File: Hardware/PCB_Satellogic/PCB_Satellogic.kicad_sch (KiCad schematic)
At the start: 4 parts, among them U1 E22-900M30S_LoRa, U2 Node-MCU_ESP32_38PINES, U3 TP4065_Modulo_cargador_de_bat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

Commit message: Introducción HW
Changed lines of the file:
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@@
-(kicad_sch (version 20211123) (generator eeschema)
+(kicad_sch (version 20230121) (generator eeschema)
   (paper "A4")
   (symbol (lib_id "Device:E22-900M30S_LoRa") (at 124.46 68.58 0) (unit 1)
-    (in_bom yes) (on_board yes)
-    (property "Reference" "U1" (id 0) (at 124.46 47.879 0))
-    (property "Value" "E22-900M30S_LoRa" (id 1) (at 124.46 50.1904 0))
-    (property "Footprint" "PCB_Satellogic:E22-900M30S_LoRa_smd" (id 2) (at 123.19 60.96 0)
+    (in_bom yes) (on_board yes) (dnp no)
+    (property "Reference" "U1" (at 124.46 47.879 0)
+      (effects (font (size 1.27 1.27)))
+    )
+    (property "Value" "E22-900M30S_LoRa" (at 124.46 50.1904 0)
+      (effects (font (size 1.27 1.27)))
+    )
+    (property "Footprint" "PCB_Satellogic:E22-900M30S_LoRa_smd" (at 123.19 60.96 0)
       (effects (font (size 1.27 1.27)) hide)
     )
-    (property "Datasheet" "" (id 3) (at 123.19 60.96 0)
+    (property "Datasheet" "" (at 123.19 60.96 0)
       (effects (font (size 1.27 1.27)) hide)
     )
@@
     (pin "8")
     (pin "9")
+    (instances
+      (project "PCB_Satellogic"
+        (path "/1c395ffa-f49b-425d-a435-d93dd675dfd0"
+          (reference "U1") (unit 1)
+        )
+      )
+    )
+  )
+  (symbol (lib_id "Diode:1N5819") (at 149.86 81.28 180) (unit 1)
+    (in_bom yes) (on_board yes) (dnp no) (fields_autoplaced)
+    (property "Reference" "D1" (at 150.1775 76.2 0)
+      (effects (font (size 1.27 1.27)))
+    )
+    (property "Value" "1N5819" (at 150.1775 78.74 0)
+      (effects (font (size 1.27 1.27)))
+    )
+    (property "Footprint" "Diode_THT:D_DO-41_SOD81_P10.16mm_Horizontal" (at 149.86 76.835 0)
+      (effects (font (size 1.27 1.27)) hide)
+    )
+    (property "Datasheet" "http://www.vishay.com/docs/88525/1n5817.pdf" (at 149.86 81.28 0)
+      (effects (font (size 1.27 1.27)) hide)
+    )
+    (pin "1")
+    (pin "2")
+    (instances
+      (project "PCB_Satellogic"
+        (path "/1c395ffa-f49b-425d-a435-d93dd675dfd0"
+          (reference "D1") (unit 1)
+        )
+      )
+    )
   )
   (symbol (lib_id "Device:Node-MCU_ESP32_38PINES") (at 172.72 57.15 0) (unit 1)
-    (in_bom yes) (on_board yes)
-    (property "Reference" "U2" (id 0) (at 172.72 28.829 0))
-    (property "Value" "Node-MCU_ESP32_38PINES" (id 1) (at 172.72 31.1404 0))
-    (property "Footprint" "PCB_Satellogic:Node-MCU_ESP32_38PINES_THT_offset" (id 2) (at 180.34 68.58 0)
+    (in_bom yes) (on_board yes) (dnp no) (fields_autoplaced)
+    (property "Reference" "U2" (at 172.72 29.21 0)
+      (effects (font (size 1.27 1.27)))
+    )
+    (property "Value" "Node-MCU_ESP32_38PINES" (at 172.72 31.75 0)
+      (effects (font (size 1.27 1.27)))
+    )
+    (property "Footprint" "PCB_Satellogic:Node-MCU_ESP32_38PINES_THT_offset" (at 180.34 68.58 0)
       (effects (font (size 1.27 1.27)) hide)
     )
-    (property "Datasheet" "" (id 3) (at 180.34 68.58 0)
+    (property "Datasheet" "" (at 180.34 68.58 0)
       (effects (font (size 1.27 1.27)) hide)
     )
@@
     (pin "8")
     (pin "9")
+    (instances
+      (project "PCB_Satellogic"
+        (path "/1c395ffa-f49b-425d-a435-d93dd675dfd0"
+          (reference "U2") (unit 1)
+        )
+      )
+    )
   )
-  (symbol (lib_id "Diode:1N5819") (at 147.32 81.28 180) (unit 1)
-    (in_bom yes) (on_board yes) (fields_autoplaced)
-    (property "Reference" "D1" (id 0) (at 147.6375 74.93 0))
-    (property "Value" "1N5819" (id 1) (at 147.6375 77.47 0))
-    (property "Footprint" "Diode_THT:D_DO-41_SOD81_P10.16mm_Horizontal" (id 2) (at 147.32 76.835 0)
+  (symbol (lib_id "Libreria_Proyecto_Satellogic:TP4065_Modulo_cargador_de_baterias") (at 72.39 73.66 0) (unit 1)
+    (in_bom yes) (on_board yes) (dnp no) (fields_autoplaced)
+    (property "Reference" "U3" (at 72.39 60.96 0)
+      (effects (font (size 1.27 1.27)))
+    )
+    (property "Value" "TP4065_Modulo_cargador_de_baterias" (at 72.39 63.5 0)
+      (effects (font (size 1.27 1.27)))
+    )
+    (property "Footprint" "PCB_Satellogic:TP4056" (at 71.12 68.58 0)
       (effects (font (size 1.27 1.27)) hide)
     )
-    (property "Datasheet" "http://www.vishay.com/docs/88525/1n5817.pdf" (id 3) (at 147.32 81.28 0)
-      (effects (font (size 1.27 1.27)) hide)
-    )
-    (pin "1")
-    (pin "2")
-  )
-  (symbol (lib_id "Libreria_Proyecto_Satellogic:TP4065_Modulo_cargador_de_baterias") (at 62.23 72.39 0) (unit 1)
-    (in_bom yes) (on_board yes) (fields_autoplaced)
-    (property "Reference" "U3" (id 0) (at 62.23 58.42 0))
-    (property "Value" "TP4065_Modulo_cargador_de_baterias" (id 1) (at 62.23 60.96 0))
-    (property "Footprint" "PCB_Satellogic:TP4056" (id 2) (at 60.96 67.31 0)
-      (effects (font (size 1.27 1.27)) hide)
-    )
-    (property "Datasheet" "" (id 3) (at 60.96 67.31 0)
+    (property "Datasheet" "" (at 71.12 68.58 0)
       (effects (font (size 1.27 1.27)) hide)
     )
@@
     (pin "5")
     (pin "6")
+    (instances
+      (project "PCB_Satellogic"
+        (path "/1c395ffa-f49b-425d-a435-d93dd675dfd0"
+          (reference "U3") (unit 1)
+        )
+      )
+    )
   )
   (sheet_instances
     (path "/" (page "1"))
   )
-  (symbol_instances
-    (path "/9dc25e6c-ccc6-4fa7-a0b9-7dc1baf8ff68"
-      (reference "D1") (unit 1) (value "1N5819") (footprint "Diode_THT:D_DO-41_SOD81_P10.16mm_Horizontal")
-    )
-    (path "/00000000-0000-0000-0000-0000640a4933"
-      (reference "U1") (unit 1) (value "E22-900M30S_LoRa") (footprint "PCB_Satellogic:E22-900M30S_LoRa_smd")
-    )
-    (path "/00000000-0000-0000-0000-0000640a5209"
-      (reference "U2") (unit 1) (value "Node-MCU_ESP32_38PINES") (footprint "PCB_Satellogic:Node-MCU_ESP32_38PINES_THT_offset")
-    )
-    (path "/db130f58-7442-4364-94e7-fd26116f26ed"
-      (reference "U3") (unit 1) (value "TP4065_Modulo_cargador_de_baterias") (footprint "PCB_Satellogic:TP4056")
-    )
-  )
 )

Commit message: Introducción HW
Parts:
- removed U2: Node-MCU_ESP32_38PINES, PCB_Satellogic:Node-MCU_ESP32_38PINES_THT_offset, symbol Device:Node-MCU_ESP32_38PINES
- added 5V_out1, BAT1, UART2: Conn_01x02, Connector_JST:JST_PH_B2B-PH-K_1x02_P2.00mm_Vertical, symbol Connector_Generic:Conn_01x02
- added U2: Node-MCU_ESP32_38PINES, PCB_Satellogic:Node-MCU_ESP32_38PINES_THT_offset, symbol Libreria_Proyecto_Satellogic:Node-MCU_ESP32_38PINES
- added U4: MT3608-Convertidor_Boost, PCB_Satellogic:MT3608-Convertidor_Boost, symbol Libreria_Proyecto_Satellogic:MT3608-Convertidor_Boost
- U3: footprint PCB_Satellogic:TP4056 -> PCB_Satellogic:TP4056 - Módulo de carga de batería
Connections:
- net GND: now reaches U1.1 (GND)
- net GND: now also U1.11 (GND), U1.12 (GND), U1.2 (GND), U1.20 (GND), U1.22 (GND), U1.3 (GND), U1.4 (GND), U1.5 (GND), 5V_out1.2 (Pin_2), U2.14 (GND), U2.38 (GND), U4.2 (VOUT-)
- net 5V: now reaches U1.10 (Vcc)
- net 5V: now also D1.2 (A), U1.9 (Vcc), 5V_out1.1 (Pin_1), U4.1 (VOUT+)
- net BUSY: now reaches U1.14 (BUSY)
- net BUSY: now also U2.33 (GPIO21)
- net RST_E22: now reaches U1.15 (NRST)
- net RST_E22: now also U2.36 (GPIO22)
- net MISO: now reaches U1.16 (MISO)
- net MISO: now also U2.31 (MISO-GPIO19)
- net MOSI: now reaches U1.17 (MOSI)
- net MOSI: now also U2.37 (MOSI-GPIO23)
- net SCK: now reaches U1.18 (SCK)
- net SCK: now also U2.30 (CLK-GPIO18)
- net NSS: now reaches U1.19 (NSS)
- net NSS: now also U2.29 (CS0-GPIO5)
- net RXEN: now reaches U1.6 (RXEN)
- net TXEN: now reaches U1.7 (TXEN)
- net at D1.1 (K): now also U2.19 (Vin)
- net at U3.3 (OUT-): now also U4.3 (VIN-)
- net BAT-: now reaches U3.4 (BAT-)
- net BAT-: now also BAT1.2 (Pin_2)
- net BAT+: now reaches U3.5 (BAT+)
- net BAT+: now also BAT1.1 (Pin_1)
- net at U3.6 (OUT+): now also U4.4 (VIN+)
- new net Rx2: U2.27 (Rx2-GPIO16), UART2.2 (Pin_2)
- new net Tx2: U2.28 (Tx2-GPIO17), UART2.1 (Pin_1)
- no-connect marks 0 -> 32
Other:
- company: (none) -> Satellogic
- title: (none) -> Esquema dispositivo de comunicación ESP32-E22
- moved on the sheet: D1, U1, U3

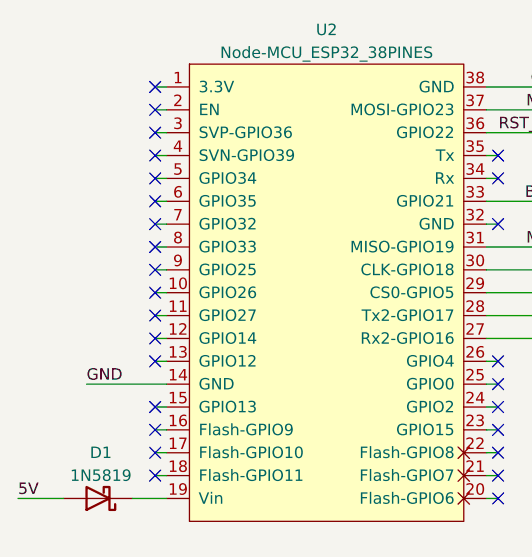
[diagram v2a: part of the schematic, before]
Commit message: Se agregó función para ver registros
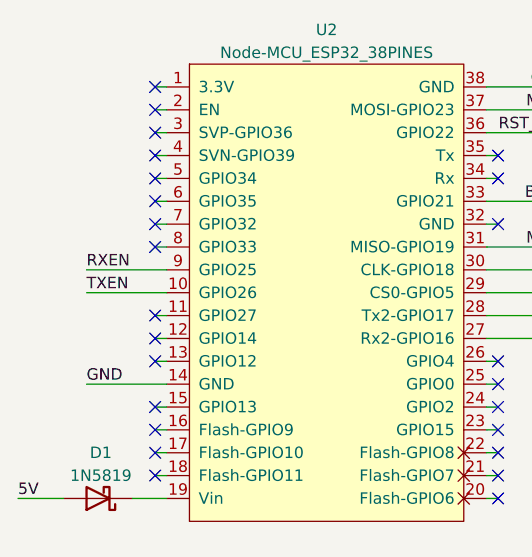
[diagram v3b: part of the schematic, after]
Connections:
- net RXEN: now also U2.9 (GPIO25)
- net TXEN: now also U2.10 (GPIO26)
- no-connect marks 32 -> 30
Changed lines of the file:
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@@
     (company "Satellogic")
   )
-  (no_connect (at 60.96 60.96))
   (no_connect (at 60.96 43.18))
   (no_connect (at 60.96 63.5))
@@
   (no_connect (at 60.96 55.88))
   (no_connect (at 99.06 76.2))
-  (no_connect (at 60.96 58.42))
   (no_connect (at 60.96 40.64))
   (no_connect (at 99.06 45.72))
@@
     (stroke (width 0) (type default))
   )
+  (wire (pts (xy 53.34 58.42) (xy 62.23 58.42))
+    (stroke (width 0) (type default))
+  )
   (wire (pts (xy 219.71 38.1) (xy 232.41 38.1))
     (stroke (width 0) (type default))
@@
     (stroke (width 0) (type default))
   )
+  (wire (pts (xy 53.34 60.96) (xy 62.23 60.96))
+    (stroke (width 0) (type default))
+  )
   (wire (pts (xy 99.06 73.66) (xy 97.79 73.66))
     (stroke (width 0) (type default))
@@
     (stroke (width 0) (type default))
   )
-  (wire (pts (xy 60.96 58.42) (xy 62.23 58.42))
-    (stroke (width 0) (type default))
-  )
   (wire (pts (xy 60.96 76.2) (xy 62.23 76.2))
     (stroke (width 0) (type default))
@@
     (stroke (width 0) (type default))
   )
-  (wire (pts (xy 60.96 60.96) (xy 62.23 60.96))
-    (stroke (width 0) (type default))
-  )
   (wire (pts (xy 97.79 63.5) (xy 106.68 63.5))
     (stroke (width 0) (type default))
@@
     (effects (font (size 1.27 1.27)) (justify left bottom))
   )
+  (label "TXEN" (at 53.34 60.96 0) (fields_autoplaced)
+    (effects (font (size 1.27 1.27)) (justify left bottom))
+  )
   (label "GND" (at 100.33 121.92 180) (fields_autoplaced)
     (effects (font (size 1.27 1.27)) (justify right bottom))
@@
     (effects (font (size 1.27 1.27)) (justify right bottom))
   )
+  (label "RXEN" (at 53.34 58.42 0) (fields_autoplaced)
+    (effects (font (size 1.27 1.27)) (justify left bottom))
+  )
   (label "GND" (at 100.33 127 180) (fields_autoplaced)

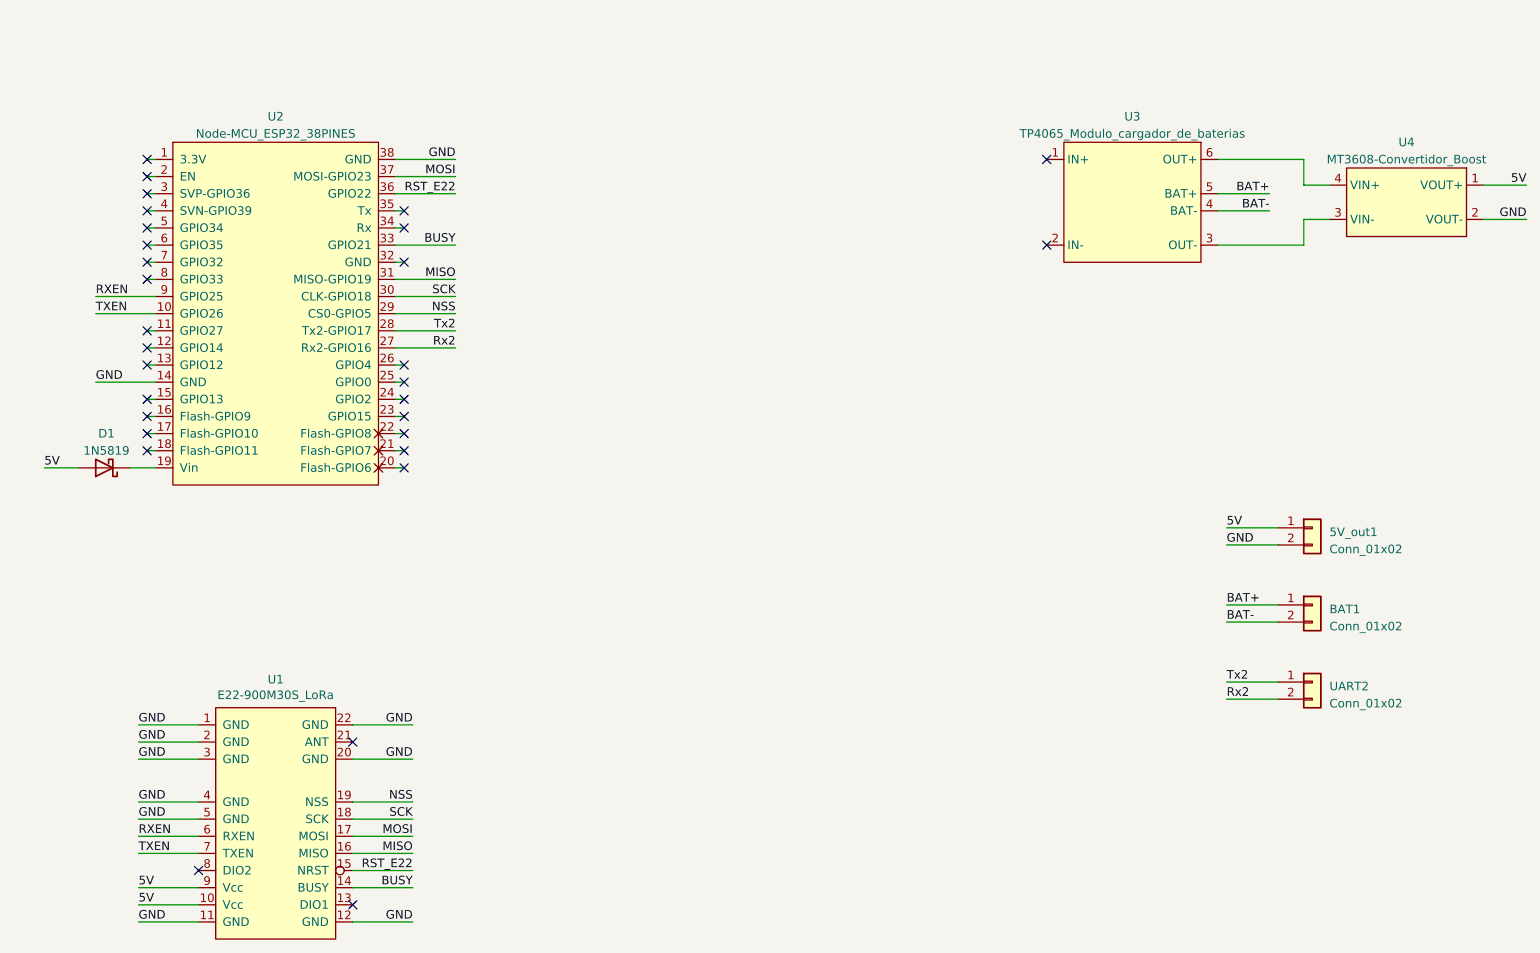
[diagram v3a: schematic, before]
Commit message: Diseño PCB 2 con I2C para pantalla OLED y pulsadores
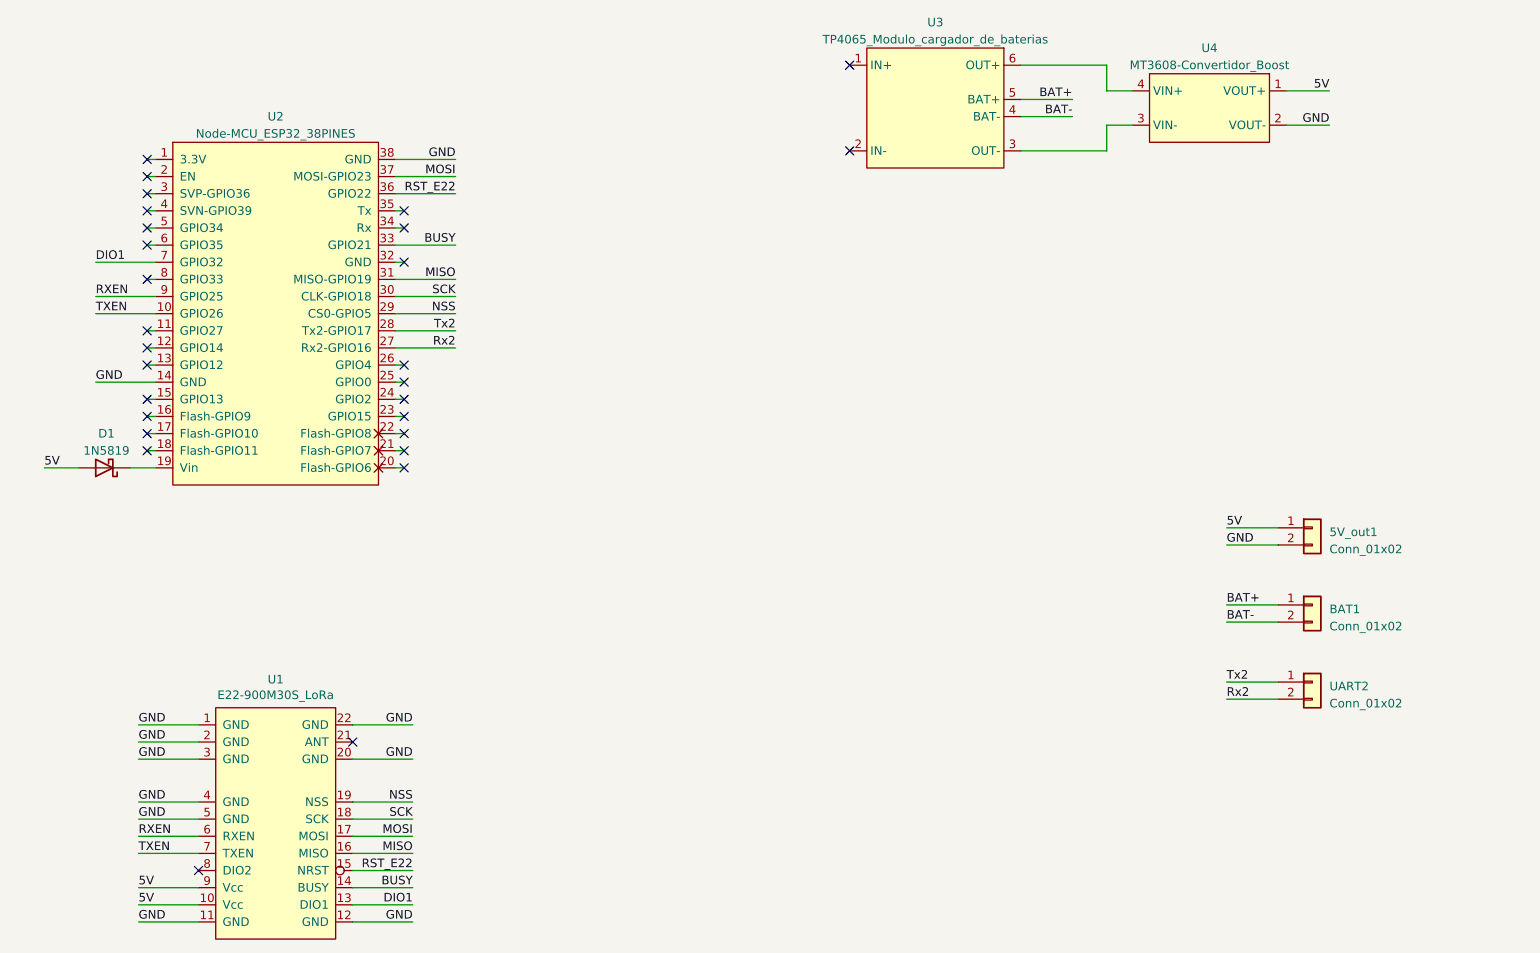
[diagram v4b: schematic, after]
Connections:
- net DIO1: now reaches U1.13 (DIO1)
- net DIO1: now also U2.7 (GPIO32)
- no-connect marks 30 -> 28
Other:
- moved on the sheet: U3, U4
